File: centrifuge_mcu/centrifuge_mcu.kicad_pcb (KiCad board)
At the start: 6 copper layers, 114 parts, among them J101 Conn_02x06_Odd_Even, J102 FPGA_Power, J103 FPGA_extra, J104 FPGA_control, J105 FPGA_SPI, J106 DDC_I2Cs, J107 ACD_I2C, J108 ACD_RST, J109 USB_B_Micro, J110 Barrel_Jack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

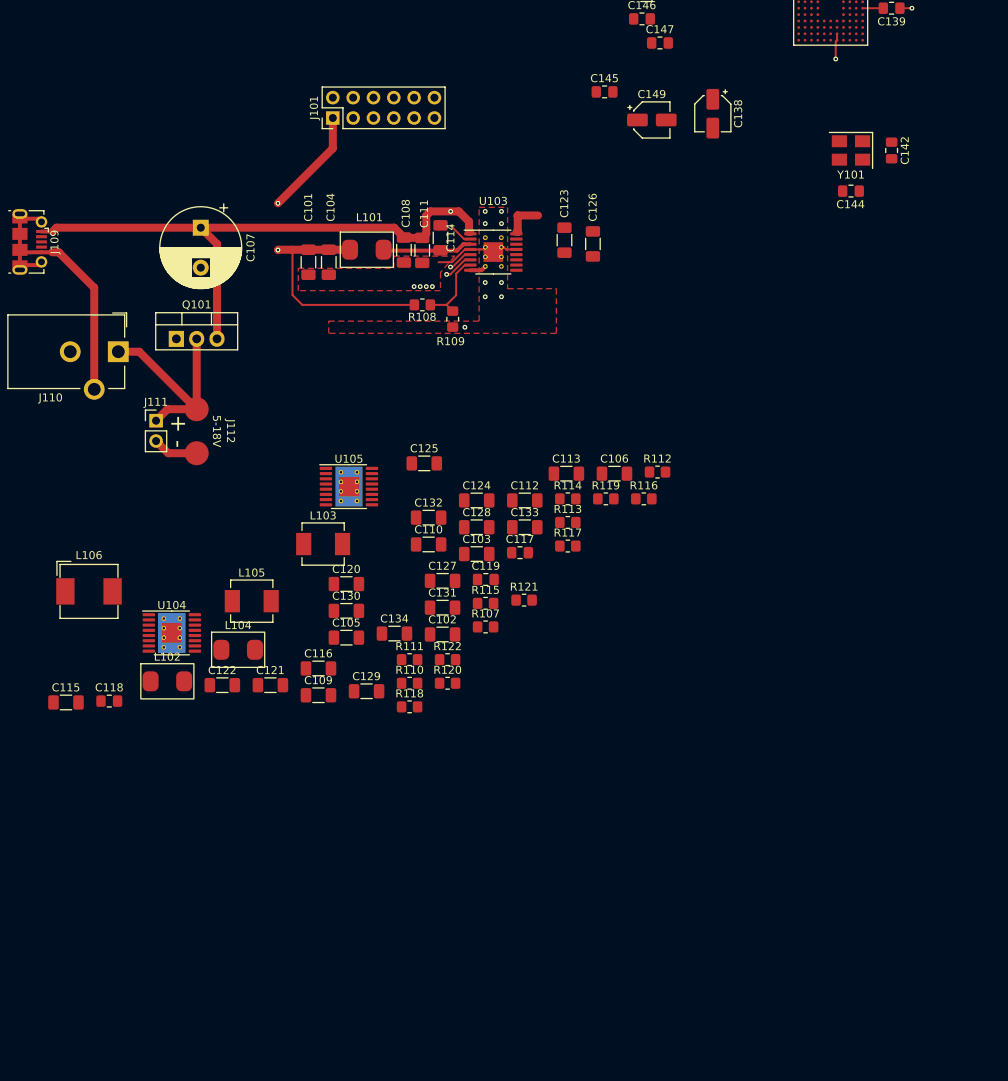
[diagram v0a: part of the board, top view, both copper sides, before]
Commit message: continue on power supply routing
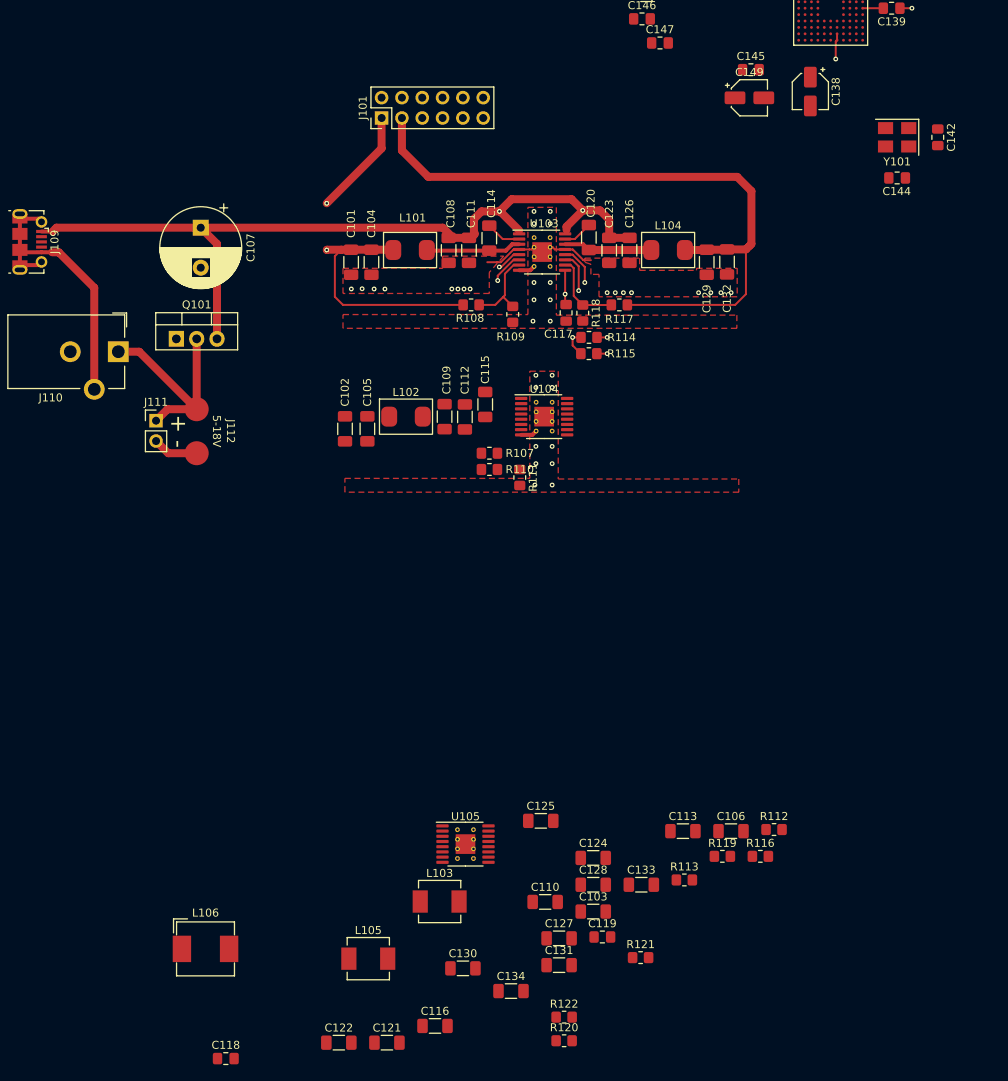
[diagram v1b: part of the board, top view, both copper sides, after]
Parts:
- moved L104 73.4 mm to (121.9, 79.8)
- moved C129 68.4 mm to (126.7, 81.3), turned to -90 degrees
- moved C115 64.3 mm to (99.1, 99.1), turned to -90 degrees
- moved U104 53.8 mm to (106.4, 100.6)
- moved R118 53.8 mm to (111.3, 87.6), turned to -90 degrees
- moved C120 52.9 mm to (112.0, 78.2), turned to -90 degrees
- moved C132 49.1 mm to (129.3, 81.2), turned to -90 degrees
- moved C110 47.0 mm to (106.6, 161.2)
- moved C116 47.0 mm to (92.8, 176.7)
- moved C118 47.0 mm to (66.6, 180.8)
- moved C119 47.0 mm to (113.7, 165.6)
- moved C121 47.0 mm to (86.8, 178.8)
- moved C122 47.0 mm to (80.8, 178.8)
- moved C124 47.0 mm to (112.6, 155.7)
- moved C128 47.0 mm to (112.6, 159.1)
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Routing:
- net /Power Circuit/1V8: track 0.00 -> 86.1 mm
- net Net-(R114-Pad2): track 3.72 -> 30.0 mm, vias 1 -> 3
- net Net-(C107-Pad1): track 88.5 -> 112.9 mm, vias 2 -> 3
- net Net-(R115-Pad2): track 0.00 -> 15.7 mm, vias 0 -> 2
- net Net-(C117-Pad2): track 0.00 -> 13.6 mm, vias 0 -> 2
- net Net-(C120-Pad2): track 0.00 -> 11.1 mm
- net Net-(R117-Pad2): track 0.00 -> 9.89 mm
- net GND: track 21.1 -> 27.0 mm, vias 15 -> 38
- net Net-(C120-Pad1): track 0.00 -> 3.69 mm
- net Net-(C114-Pad1): track 3.15 -> 5.11 mm
- net Net-(C114-Pad2): track 11.2 -> 12.6 mm
- net /Power Circuit/1V0: track 49.8 -> 50.4 mm
- net Net-(R108-Pad2): track 9.74 -> 10.3 mm

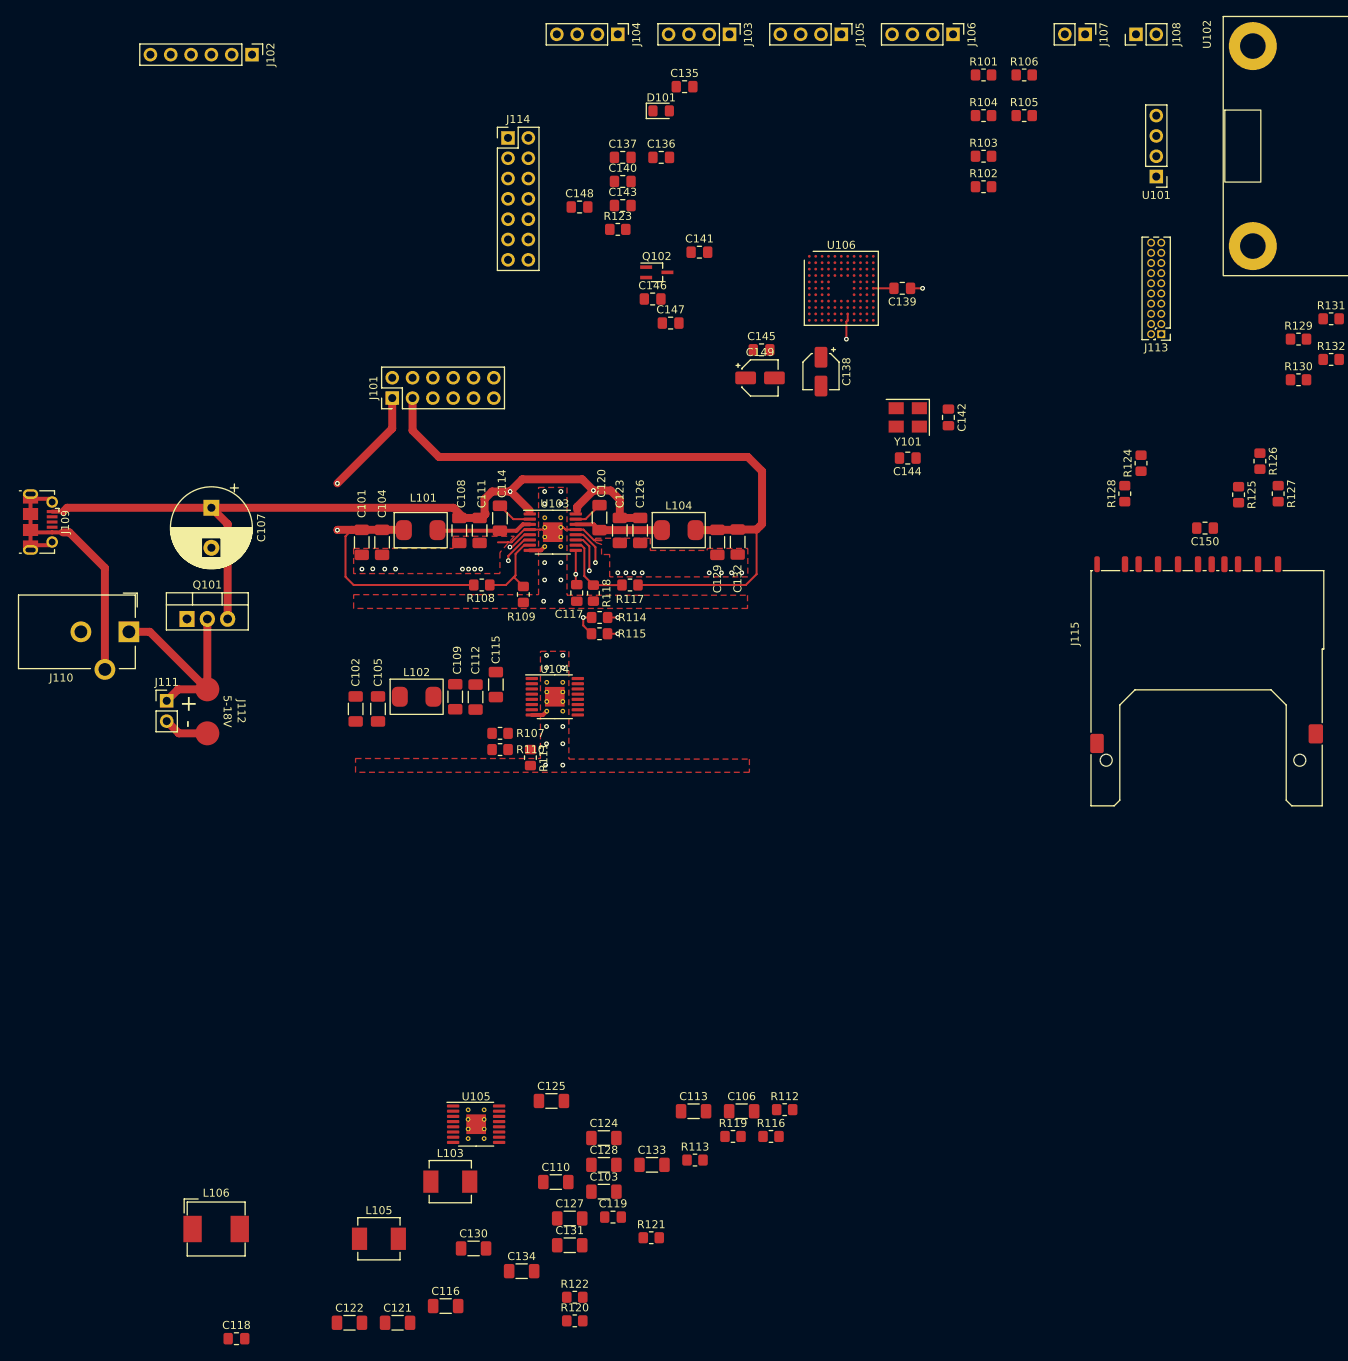
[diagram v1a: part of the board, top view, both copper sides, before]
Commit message: slowly but surely decopling and connecting everything to the MCU
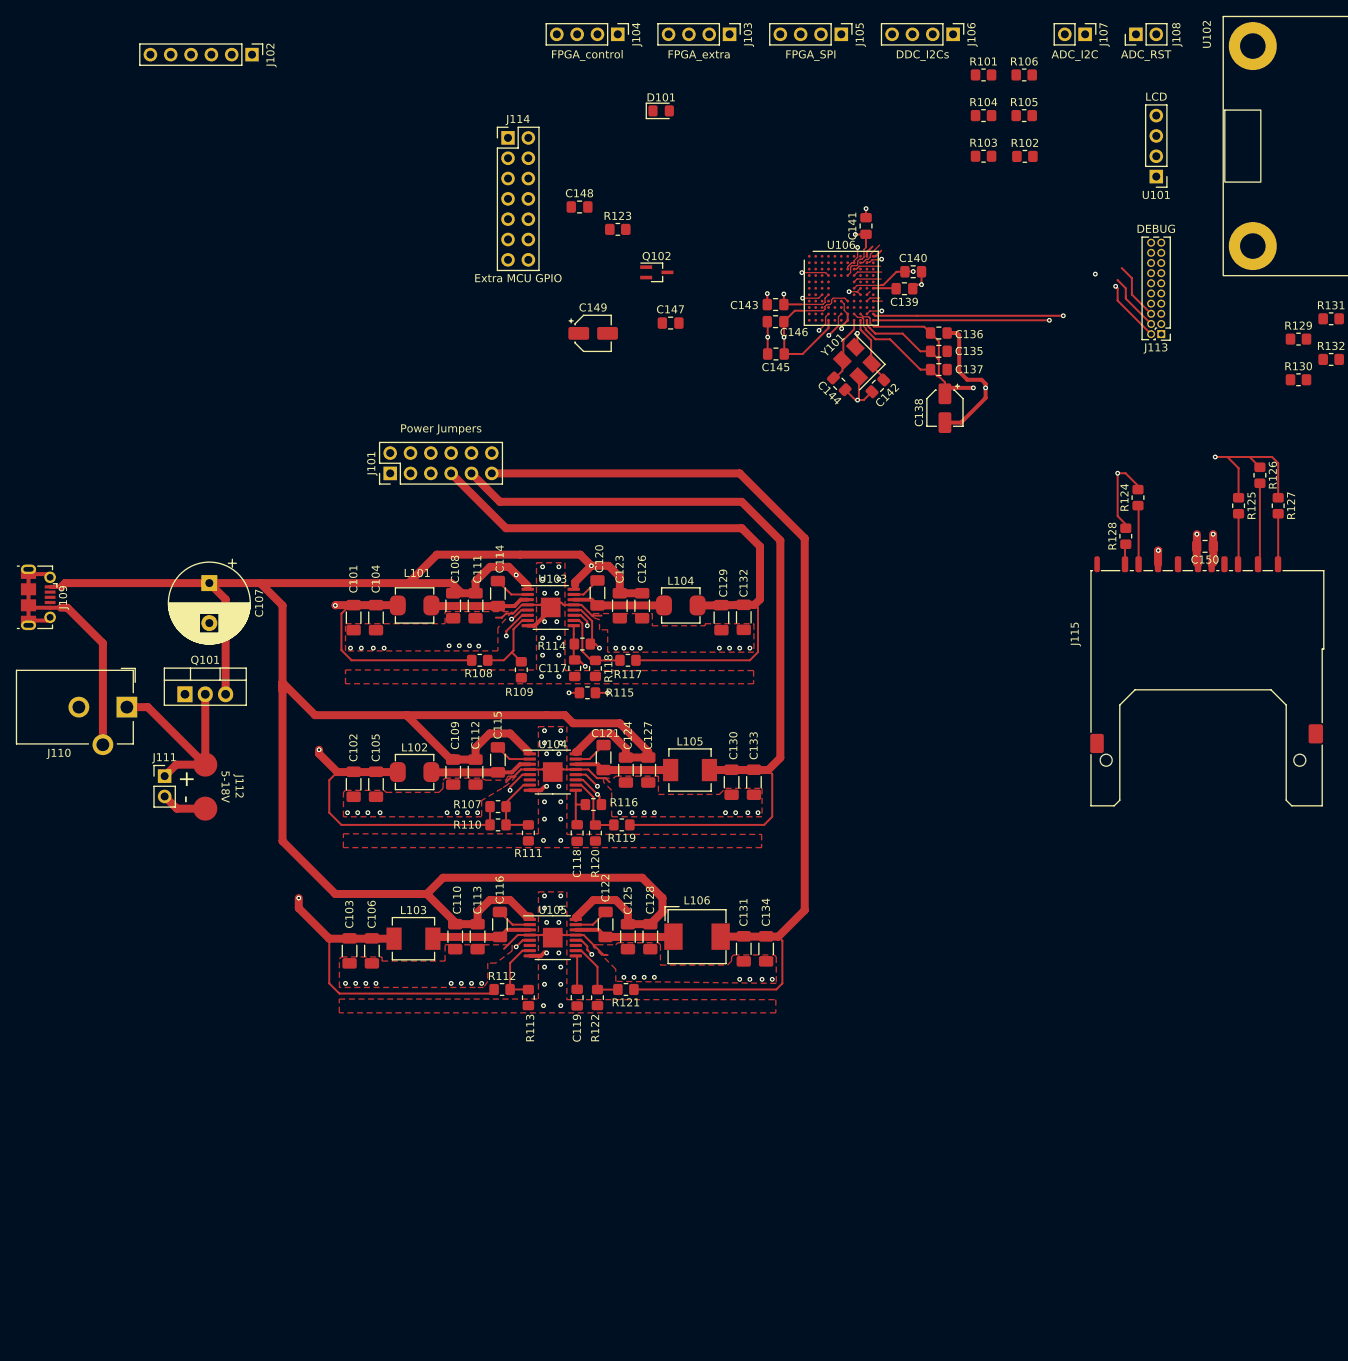
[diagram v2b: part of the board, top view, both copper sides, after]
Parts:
- J101: value Conn_02x06_Odd_Even -> Power Jumpers
- J107: value ACD_I2C -> ADC_I2C
- J108: value ACD_RST -> ADC_RST
- J113: value Conn_02x10_Odd_Even -> DEBUG
- U101: value DFR0555 -> LCD
- moved C118 76.2 mm to (109.2, 117.6), turned to 90 degrees
- moved C121 75.2 mm to (112.5, 108.2), turned to -90 degrees
- moved L106 70.3 mm to (124.2, 130.6)
- moved L105 70.3 mm to (123.3, 109.7)
- moved C130 66.6 mm to (128.5, 111.3), turned to -90 degrees
- moved R120 61.0 mm to (111.5, 117.6), turned to -90 degrees
- moved C122 59.2 mm to (112.8, 129.0), turned to -90 degrees
- moved C127 56.9 mm to (118.1, 109.7), turned to -90 degrees
- moved C134 50.6 mm to (132.8, 132.1), turned to -90 degrees
- moved C106 50.4 mm to (83.6, 132.3), turned to -90 degrees
- moved C133 49.5 mm to (131.3, 111.3), turned to -90 degrees
- moved C116 48.2 mm to (99.6, 129.0), turned to -90 degrees
- moved C137 47.6 mm to (154.4, 59.7)
- moved R116 47.1 mm to (111.3, 114.1)
- moved C124 46.1 mm to (115.3, 109.7), turned to -90 degrees
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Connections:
- J101 pad 1: /Power Circuit/1V0 -> /Power Circuit/3V3ADC
- J101 pad 10: +3.3VADC -> +3.3V
- J101 pad 2: +1V0 -> +3.3VADC
- J101 pad 3: /Power Circuit/1V8 -> /Power Circuit/1V9
- J101 pad 4: +1V8 -> +1V9
- J101 pad 5: /Power Circuit/3V3 -> /Power Circuit/1V0
- J101 pad 6: +3.3V -> +1V0
- J101 pad 7: /Power Circuit/1V9 -> /Power Circuit/1V8
- J101 pad 8: +1V9 -> +1V8
- J101 pad 9: /Power Circuit/3V3ADC -> /Power Circuit/3V3
- J102 pad 2: +3.3VADC -> +3.3V
- J102 pad 3: +1V9 -> +1V8
- J102 pad 4: +3.3V -> +1V0
- J102 pad 5: +1V8 -> +1V9
- J102 pad 6: +1V0 -> +3.3VADC
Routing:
- net Net-(C107-Pad1): track 112.9 -> 326.5 mm
- net +3.3V: track 0.00 -> 128.6 mm, vias 0 -> 8
- net /Power Circuit/5V0: track 0.00 -> 125.8 mm
- net /Power Circuit/3V3: track 0.00 -> 103.0 mm
- net /Power Circuit/3V3ADC: track 0.00 -> 101.4 mm, vias 0 -> 1
- net GND: track 27.0 -> 116.6 mm, vias 38 -> 107
- net /Power Circuit/1V9: track 0.00 -> 80.6 mm, vias 0 -> 1
- net Net-(J113-Pad10): track 0.00 -> 67.9 mm, vias 0 -> 1
- net /MCU/ADC1_RST: track 0.00 -> 63.8 mm, vias 0 -> 1
- net Net-(R116-Pad2): track 0.00 -> 62.4 mm, vias 0 -> 4
- net /MCU/ADC0_RST: track 0.00 -> 62.2 mm, vias 0 -> 1
- net Net-(J113-Pad2): track 0.00 -> 14.6 mm, vias 0 -> 2
- net Net-(R115-Pad2): track 15.7 -> 29.9 mm, vias 2 -> 3
- net Net-(C115-Pad2): track 0.00 -> 12.7 mm
- net Net-(C122-Pad2): track 0.00 -> 12.6 mm
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- added copper zone on In3.Cu, net +3.3V

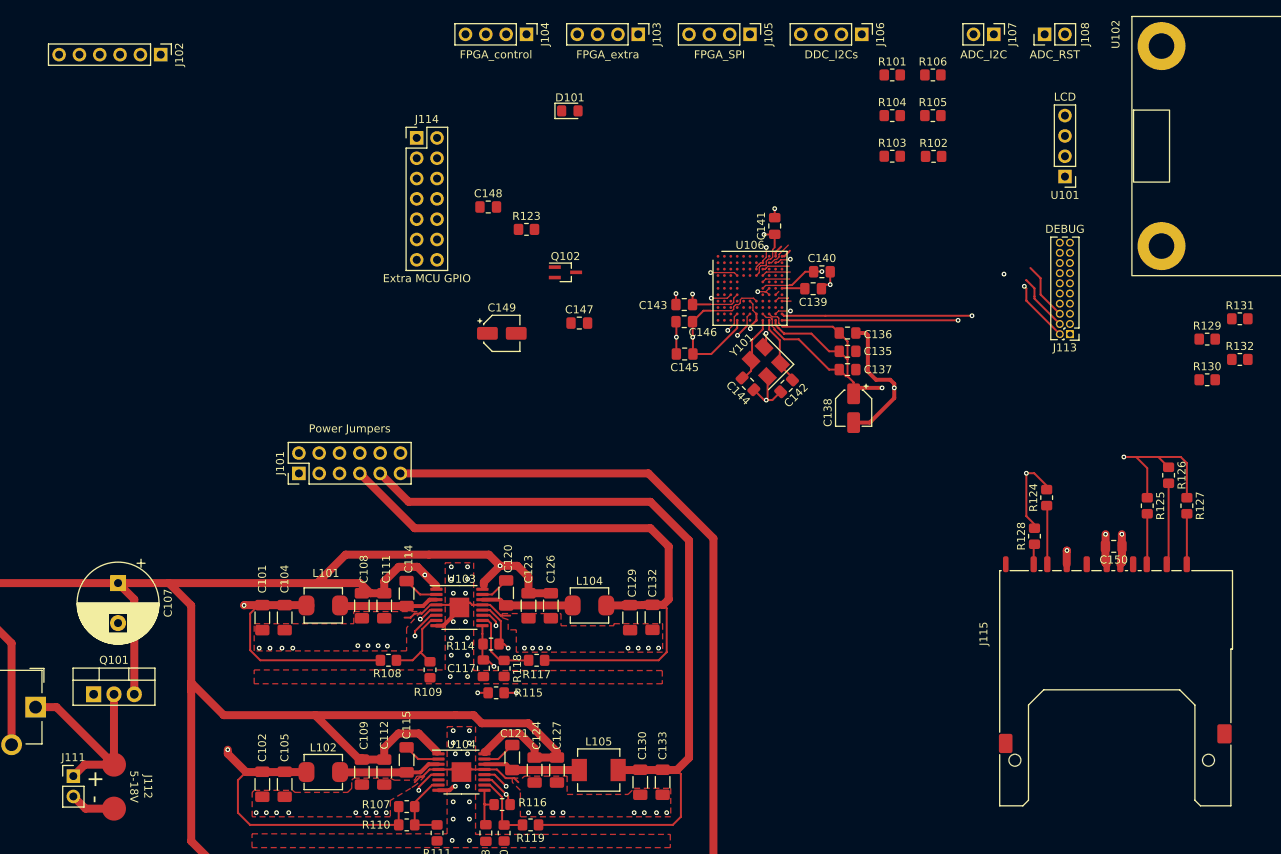
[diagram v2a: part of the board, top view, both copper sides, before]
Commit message: hooking things up to the MCU, maybe we could even make the board a bit smaller
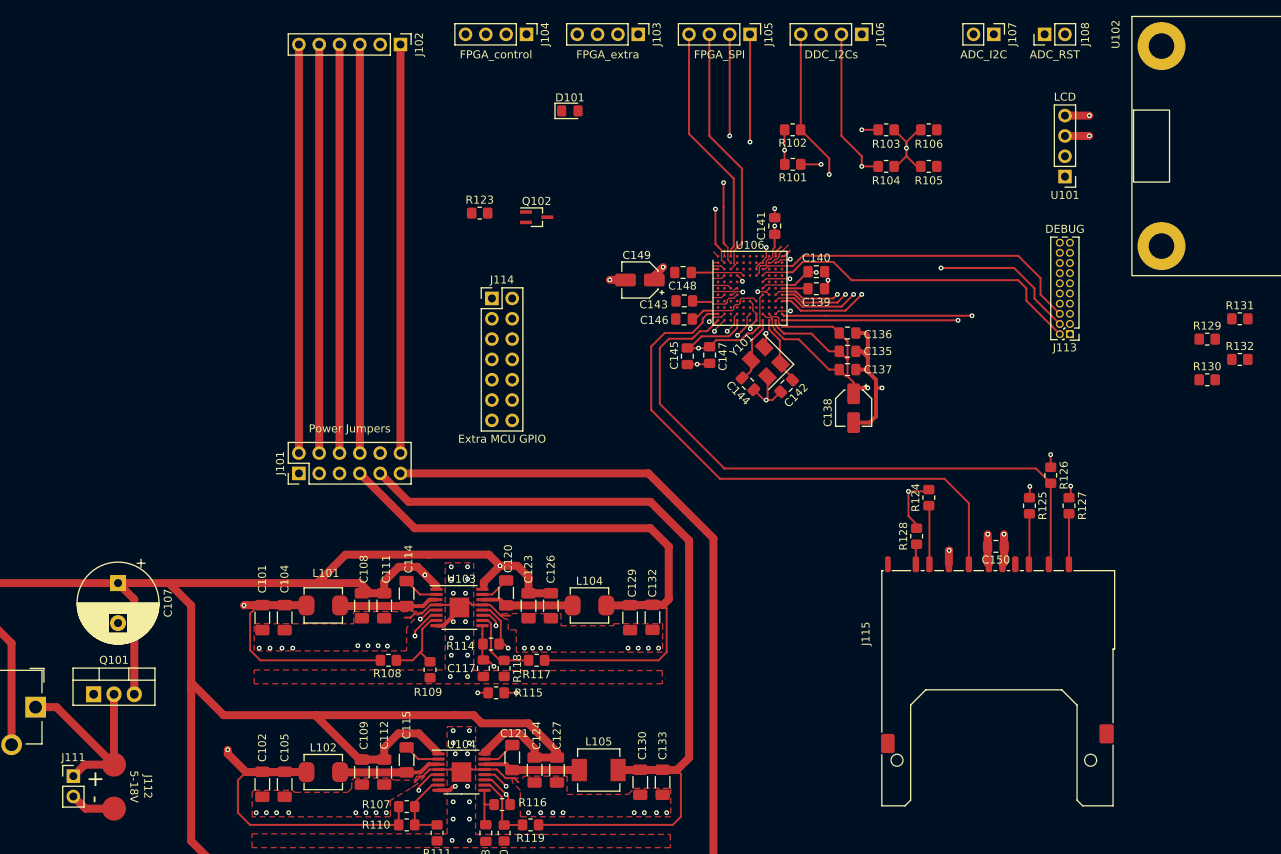
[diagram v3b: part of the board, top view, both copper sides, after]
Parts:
- moved J102 30.0 mm to (98.6, 19.1)
- moved C148 25.7 mm to (133.9, 47.5), turned to 180 degrees
- moved J114 22.2 mm to (110.0, 50.8)
- moved C149 18.5 mm to (128.5, 48.5), turned to 180 degrees
- moved R102 17.9 mm to (147.6, 29.7), turned to 180 degrees
- moved C147 16.8 mm to (137.2, 57.9), turned to -90 degrees
- moved R101 16.7 mm to (147.6, 34.0), turned to 180 degrees
- moved C150 14.7 mm to (173.0, 81.8)
- moved J115 14.7 mm to (172.7, 96.5)
- moved R124 14.7 mm to (164.6, 75.7)
- moved R125 14.7 mm to (177.2, 76.7)
- moved R126 14.7 mm to (179.8, 72.9)
- moved R127 14.7 mm to (182.1, 76.7)
- moved R128 14.7 mm to (163.1, 80.5)
- moved Q102 7.78 mm to (115.6, 40.6)
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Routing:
- net /MCU/SPI1_CLK: track 0.00 -> 70.4 mm
- net /MCU/SPI1_CS: track 10.2 -> 78.9 mm
- net +3.3V: track 128.6 -> 194.0 mm, vias 8 -> 13
- net +5V: track 0.00 -> 51.1 mm
- net +3.3VADC: track 0.00 -> 51.1 mm
- net +1V9: track 0.00 -> 51.1 mm
- net +1V8: track 0.00 -> 51.1 mm
- net +1V0: track 0.00 -> 51.1 mm
- net /MCU/I2C0_SCL#1: track 1.14 -> 46.9 mm, vias 0 -> 2
- net /MCU/I2C0_SDA#1: track 1.76 -> 46.0 mm, vias 0 -> 2
- net /MCU/I2C0_SDA#2: track 0.57 -> 44.4 mm, vias 0 -> 2
- net /MCU/I2C0_SCL#2: track 0.00 -> 43.6 mm, vias 0 -> 2
- net Net-(J113-Pad4): track 10.7 -> 42.5 mm, vias 0 -> 2
- net /MCU/SPI0_MOSI: track 0.00 -> 31.7 mm
- net Net-(J113-Pad6): track 10.7 -> 42.0 mm
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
